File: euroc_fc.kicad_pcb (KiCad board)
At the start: 4 copper layers, 50 x 100 mm, 123 parts, among them J1 Micro-Fit, J10 USB_C_Receptacle_USB2.0, J2 Micro-Fit, J3 Micro-Fit, J4 SMA, J5 JST-GH, J6 JST-GH, J7 JST-GH, J8 JST-GH, J9 Micro_SD_Card_Det, Q1 DMN2056U, Q2 AOSP21321, Q3 DMN2056U, Q4 AOSP21321, Q5 DMN2056U, Q6 DMN2056U, Q7 DMN2056U, SW1 EVQ-PUC02K, SW2 EVQ-PUC02K, U1 STM32F401RCT6, U10 Ai-Thinker-Ra-01, U11 W25Q256JVF, U2 L7805, U3 L7805, U4 AZ1117I-3.3, U5 LSM6DSR, U6 ADXL375, U7 MS5611-01BA, U8 BMM150, U9 SAM-M8Q, Y1 25M

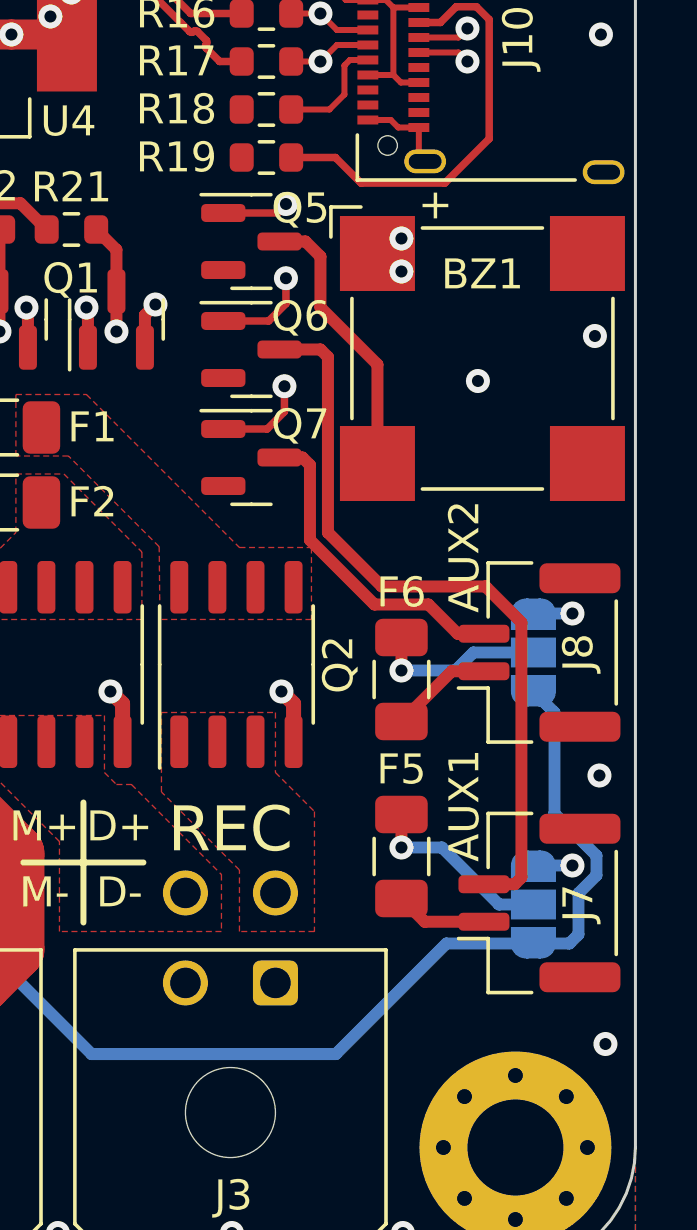
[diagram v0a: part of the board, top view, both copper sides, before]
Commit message: Add flyback diode for buzzer
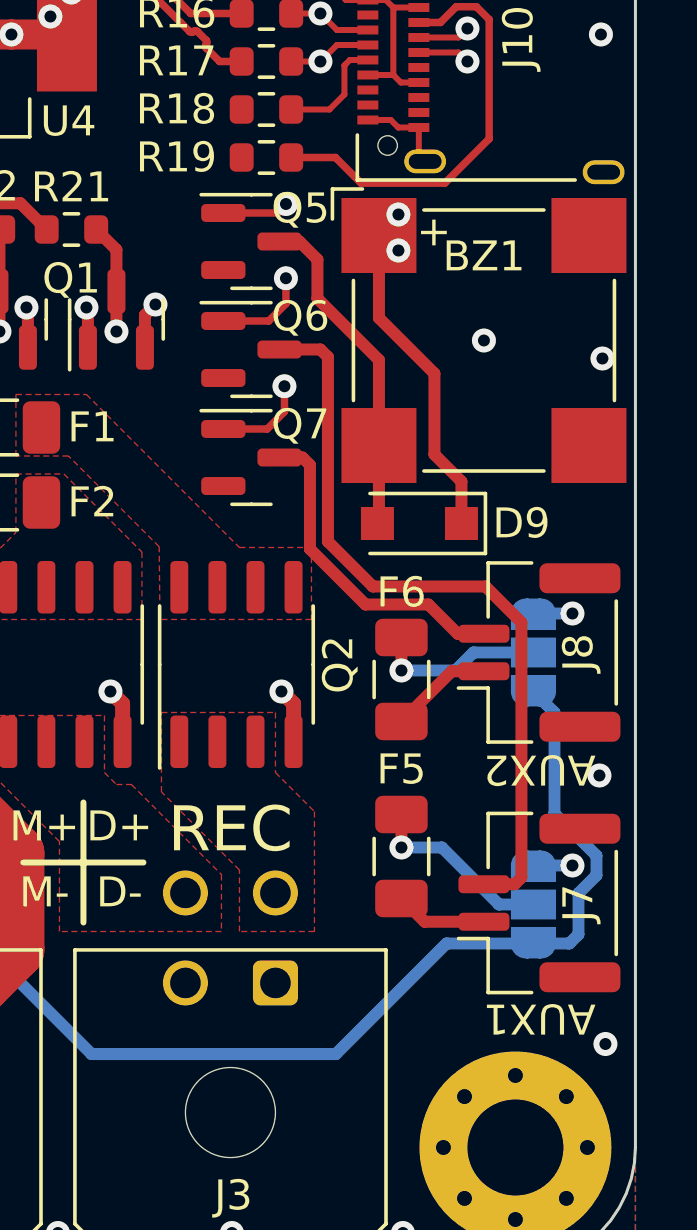
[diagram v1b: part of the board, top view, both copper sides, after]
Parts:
- added D9: SS26FL, Diode_SMD:D_SOD-123F, F.Cu at (117.8, 125.2)
- moved BZ1 0.60 mm to (120.0, 119.1)
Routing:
- net +5V: track 15.0 -> 25.7 mm
- net Net-(BZ1-Pad2): track 9.26 -> 11.2 mm

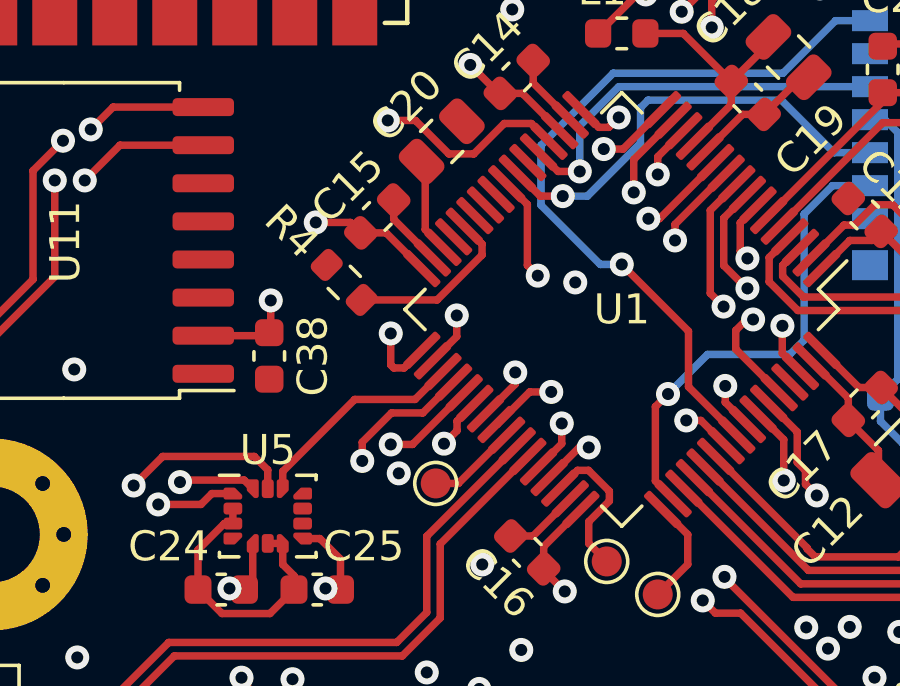
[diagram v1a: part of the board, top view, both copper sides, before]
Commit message: Fix ADC pin assignment, rename nets
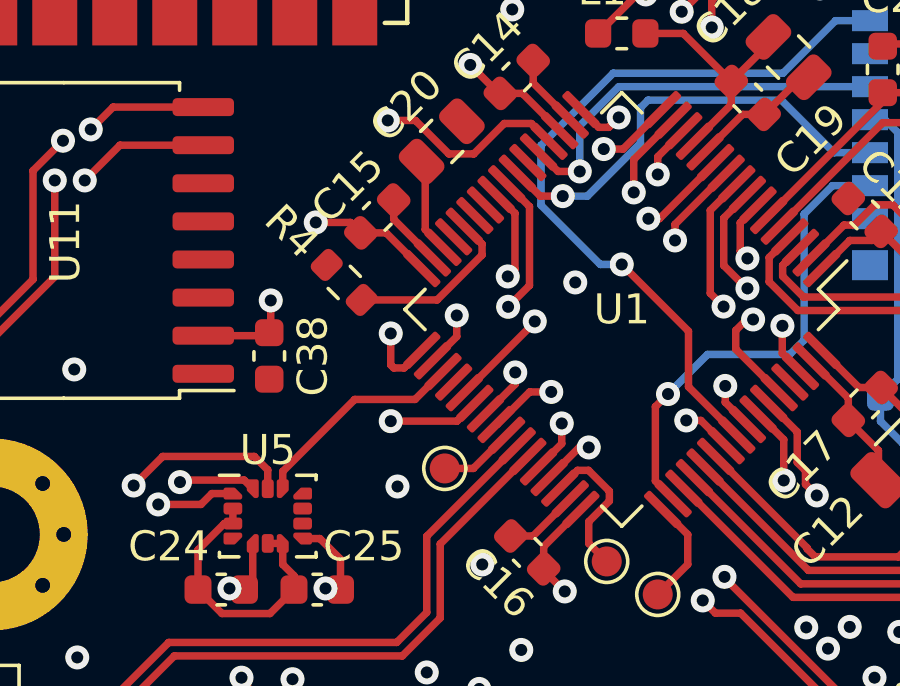
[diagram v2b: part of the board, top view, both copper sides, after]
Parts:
- moved TP1 0.58 mm to (94.1, 97.8)
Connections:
- net SPI2_CS_ACC2 renamed SPI3_CS_ACC2
- net SPI3_CS_FLASH renamed SPI2_CS_FLASH
- J5 pad 2: UART2_TX -> UART1_TX
- J5 pad 3: UART2_RX -> UART1_RX
- L2 pad 2: UART1_TX -> UART2_TX
- L3 pad 2: UART1_RX -> UART2_RX
- U1 pad 10: SPI3_MISO -> SPI2_MISO
- U1 pad 11: SPI3_MOSI -> SPI2_MOSI
- U1 pad 16: UART1_TX -> UART2_TX
- U1 pad 17: UART1_RX -> UART2_RX
- U1 pad 24: SPI1_CS_BARO -> ADC_BAT_LOW
- U1 pad 25: unconnected-(U1-Pad25) -> ADC_BAT_HIGH
- U1 pad 34: SPI3_SCL -> SPI2_SCL
- U1 pad 36: ADC_BAT_LOW -> unconnected-(U1-Pad36)
- U1 pad 37: ADC_BAT_HIGH -> SPI1_CS_BARO
- U1 pad 42: UART2_TX -> UART1_TX
- U1 pad 43: UART2_RX -> UART1_RX
- U1 pad 51: SPI2_SCL -> SPI3_SCL
- U1 pad 52: SPI2_MISO -> SPI3_MISO
- U1 pad 53: SPI2_MOSI -> SPI3_MOSI
- U11 pad 15: SPI3_MOSI -> SPI2_MOSI
- U11 pad 16: SPI3_SCL -> SPI2_SCL
- U11 pad 8: SPI3_MISO -> SPI2_MISO
- U6 pad 12: SPI2_MISO -> SPI3_MISO
- U6 pad 13: SPI2_MOSI -> SPI3_MOSI
- U6 pad 14: SPI2_SCL -> SPI3_SCL
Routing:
- net SPI3_MOSI: track 34.8 -> 14.1 mm, vias 2 -> 0
- net SPI2_MOSI: track 14.1 -> 34.8 mm, vias 0 -> 2
- net SPI3_MISO: track 28.4 -> 14.5 mm
- net SPI2_MISO: track 14.5 -> 28.4 mm
- net SPI3_SCL: track 27.3 -> 15.5 mm, vias 2 -> 0
- net SPI2_SCL: track 15.5 -> 27.3 mm, vias 0 -> 2
- net ADC_BAT_LOW: track 35.1 -> 42.5 mm
- net UART2_RX: track 24.1 -> 17.4 mm, vias 0 -> 2
- net UART1_RX: track 17.4 -> 24.1 mm, vias 2 -> 0
- net ADC_BAT_HIGH: track 37.2 -> 42.9 mm
- net UART2_TX: track 23.4 -> 20.6 mm, vias 0 -> 2
- net UART1_TX: track 20.6 -> 23.4 mm, vias 2 -> 0
- net SPI1_CS_MAG: track 17.1 -> 15.0 mm
- net SPI1_CS_BARO: track 23.1 -> 24.5 mm
- net MCO1: track 3.03 -> 2.52 mm

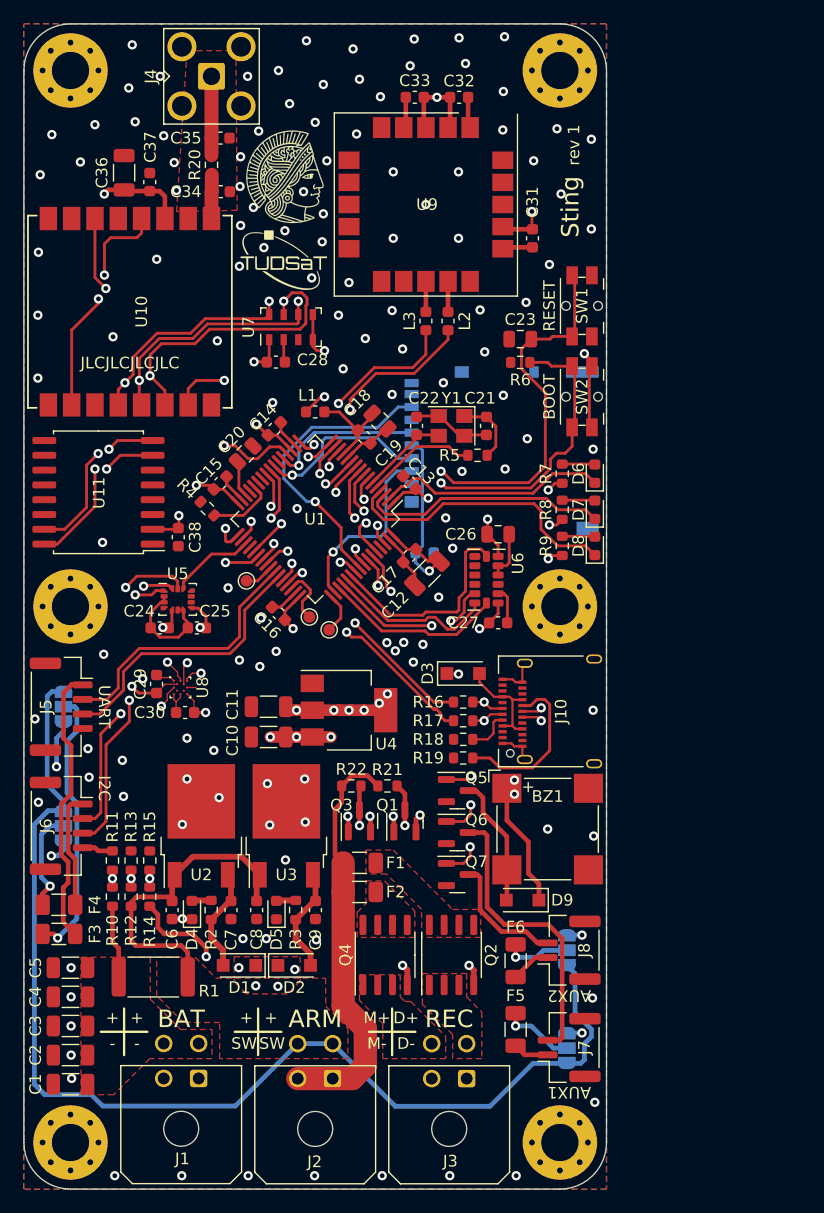
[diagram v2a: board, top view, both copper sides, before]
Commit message: Place additional test points
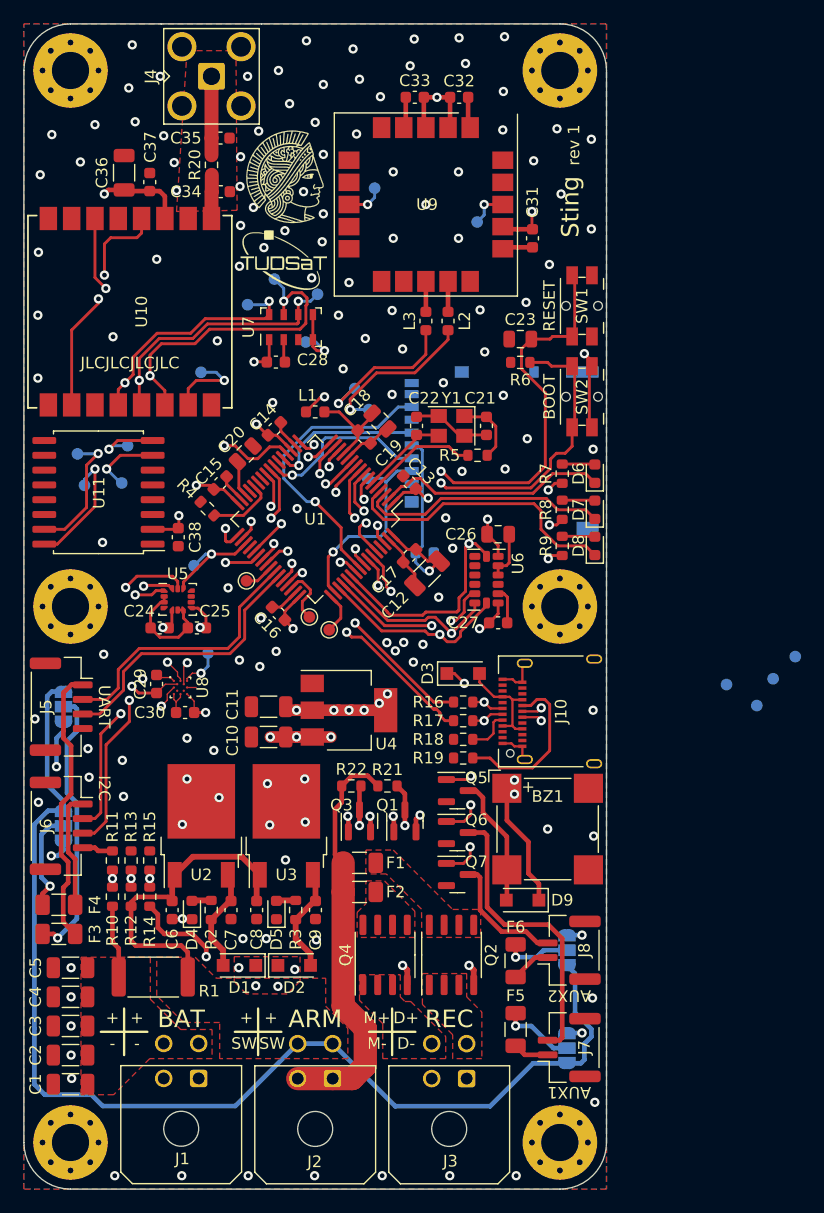
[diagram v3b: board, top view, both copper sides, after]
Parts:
- added TP10: TestPoint, TestPoint:TestPoint_Pad_D1.0mm, B.Cu at (90.2, 79.9)
- added TP11: TestPoint, TestPoint:TestPoint_Pad_D1.0mm, B.Cu at (104.5, 89.0)
- added TP12: TestPoint, TestPoint:TestPoint_Pad_D1.0mm, B.Cu at (80.2, 89.6)
- added TP13: TestPoint, TestPoint:TestPoint_Pad_D1.0mm, B.Cu at (79.6, 86.9)
- added TP14: TestPoint, TestPoint:TestPoint_Pad_D1.0mm, B.Cu at (83.9, 86.2)
- added TP15: TestPoint, TestPoint:TestPoint_Pad_D1.0mm, B.Cu at (83.4, 89.4)
- added TP16: TestPoint, TestPoint:TestPoint_Pad_D1.0mm, B.Cu at (139.3, 106.2)
- added TP17: TestPoint, TestPoint:TestPoint_Pad_D1.0mm, B.Cu at (137.9, 108.5)
- added TP18: TestPoint, TestPoint:TestPoint_Pad_D1.0mm, B.Cu at (141.2, 104.3)
- added TP19: TestPoint, TestPoint:TestPoint_Pad_D1.0mm, B.Cu at (135.3, 106.7)
- added TP20: TestPoint, TestPoint:TestPoint_Pad_D1.0mm, B.Cu at (104.6, 83.1)
- added TP21: TestPoint, TestPoint:TestPoint_Pad_D1.0mm, B.Cu at (103.4, 81.3)
- added TP22: TestPoint, TestPoint:TestPoint_Pad_D1.0mm, B.Cu at (105.1, 64.1)
- added TP23: TestPoint, TestPoint:TestPoint_Pad_D1.0mm, B.Cu at (113.9, 67.0)
- added TP4: TestPoint, TestPoint:TestPoint_Pad_D1.0mm, B.Cu at (94.2, 74.1)
- added TP5: TestPoint, TestPoint:TestPoint_Pad_D1.0mm, B.Cu at (96.5, 71.9)
- added TP6: TestPoint, TestPoint:TestPoint_Pad_D1.0mm, B.Cu at (100.2, 73.2)
- added TP7: TestPoint, TestPoint:TestPoint_Pad_D1.0mm, B.Cu at (89.6, 96.5)
- added TP8: TestPoint, TestPoint:TestPoint_Pad_D1.0mm, B.Cu at (90.8, 104.0)
- added TP9: TestPoint, TestPoint:TestPoint_Pad_D1.0mm, B.Cu at (99.2, 77.3)
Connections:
- U9 pad 18: unconnected-(U9-Pad18) -> GPS_RESET
- U9 pad 8: unconnected-(U9-Pad8) -> GPS_SAFEBOOT
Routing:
- net GPS_RESET: track 0.00 -> 3.35 mm, vias 0 -> 1
- net GPS_SAFEBOOT: track 0.00 -> 3.25 mm, vias 0 -> 1
- net SPI1_CS_RADIO: track 24.8 -> 27.1 mm
- net SPI1_MOSI: track 92.8 -> 95.0 mm
- net SPI1_SCL: track 82.4 -> 84.4 mm
- net SPI1_CS_MAG: track 15.0 -> 17.0 mm
- net UART2_RX: track 17.4 -> 19.3 mm
- net SPI1_CS_ACC1: track 7.30 -> 9.21 mm, vias 0 -> 1
- net SPI1_CS_BARO: track 24.5 -> 26.4 mm
- net SPI1_MISO: track 105.0 -> 106.8 mm
- net SPI2_CS_FLASH: track 22.6 -> 24.4 mm
- net SPI2_MOSI: track 34.8 -> 36.6 mm
- net SPI2_SCL: track 27.3 -> 29.1 mm
- net SPI2_MISO: track 28.4 -> 30.1 mm
- net SPI1_CS_SD: track 16.0 -> 17.7 mm
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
